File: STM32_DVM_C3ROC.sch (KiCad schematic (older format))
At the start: 174 parts, among them IC2 MCP6002, IC3 MCP6002, IC4 MCP6002, J1 40HAT, J2 USB_B_Micro, Q1 Crystal_GND24, SW1 SW_Push, T1 MMUN2214, T2 MMUN2214, T3 MMUN2214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

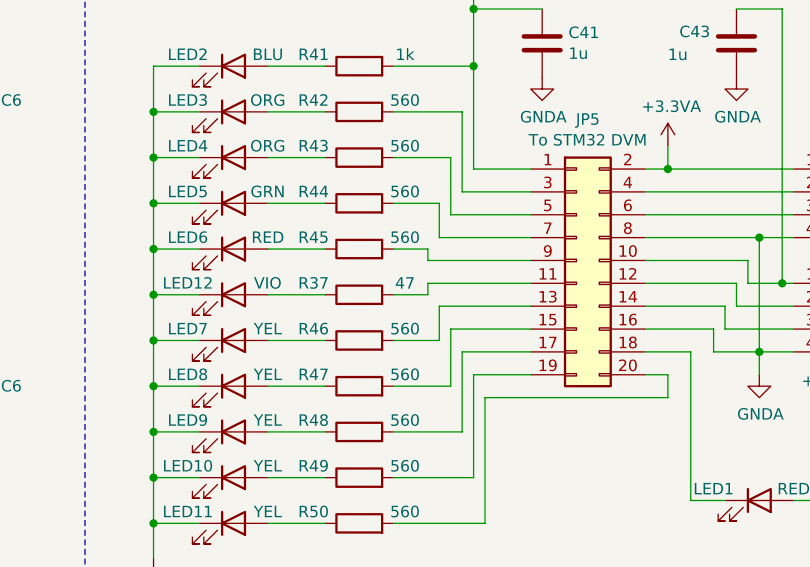
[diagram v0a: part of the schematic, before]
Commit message: Layout fertig, Produktionsdaten für JCLPCB erzeugt
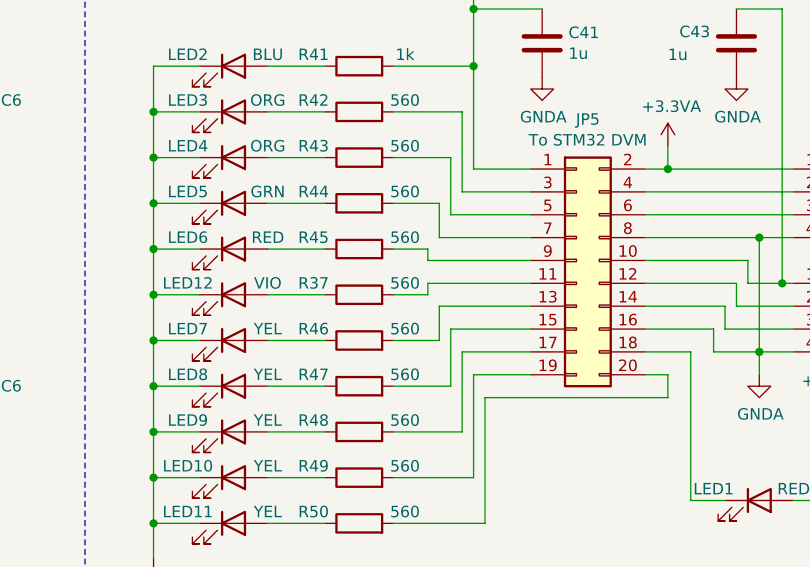
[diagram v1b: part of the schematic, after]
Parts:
- R37: value 47 -> 560
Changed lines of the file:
@@
 P 12900 2600
 F 0 "R37" V 12950 2800 50  0000 C CNN
-F 1 "47" V 12950 2400 50  0000 C CNN
+F 1 "560" V 12950 2400 50  0000 C CNN
 F 2 "Resistor_SMD:R_0603_1608Metric" V 12830 2600 50  0001 C CNN
 F 3 "" H 12900 2600 50  0001 C CNN
